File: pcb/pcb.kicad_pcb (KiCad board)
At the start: 2 copper layers, 132 x 228 mm, 54 parts, among them J1 GPS Module Breakout, J2 MicroSD Card Breakout, J3 I2C Display, J4 Exhaust Fan, U1 XIAO-ESP32-C5-DIP, U10 XIAO-ESP32-C5-DIP, U11 XIAO-ESP32-C5-DIP, U12 XIAO-ESP32-C5-DIP, U13 XIAO-ESP32-C5-DIP, U14 XIAO-ESP32-C5-DIP, U15 XIAO-ESP32-C5-DIP, U16 XIAO-ESP32-C5-DIP, U17 ESP32-S3 DevKitC-1, U18 LD1117V33, U19 SN74HC125N, U2 XIAO-ESP32-C5-DIP, U20 SN74HC138N, U21 SN74HC138N, U3 XIAO-ESP32-C5-DIP, U4 XIAO-ESP32-C5-DIP, U5 XIAO-ESP32-C5-DIP, U6 XIAO-ESP32-C5-DIP, U7 XIAO-ESP32-C5-DIP, U8 XIAO-ESP32-C5-DIP, U9 XIAO-ESP32-C5-DIP

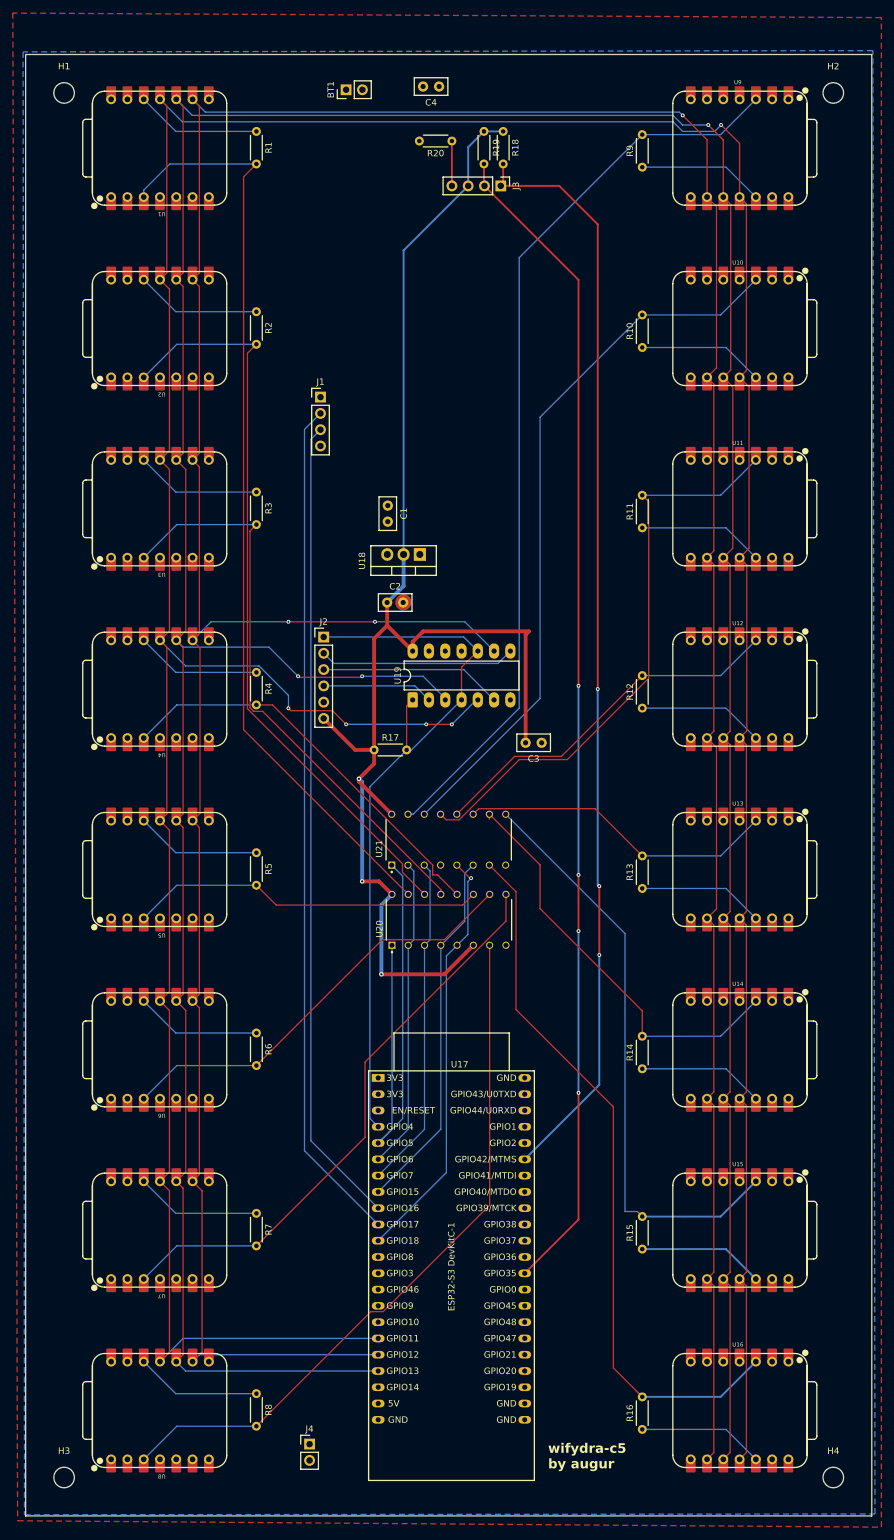
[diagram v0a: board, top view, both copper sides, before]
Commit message: Increasing ordered magic
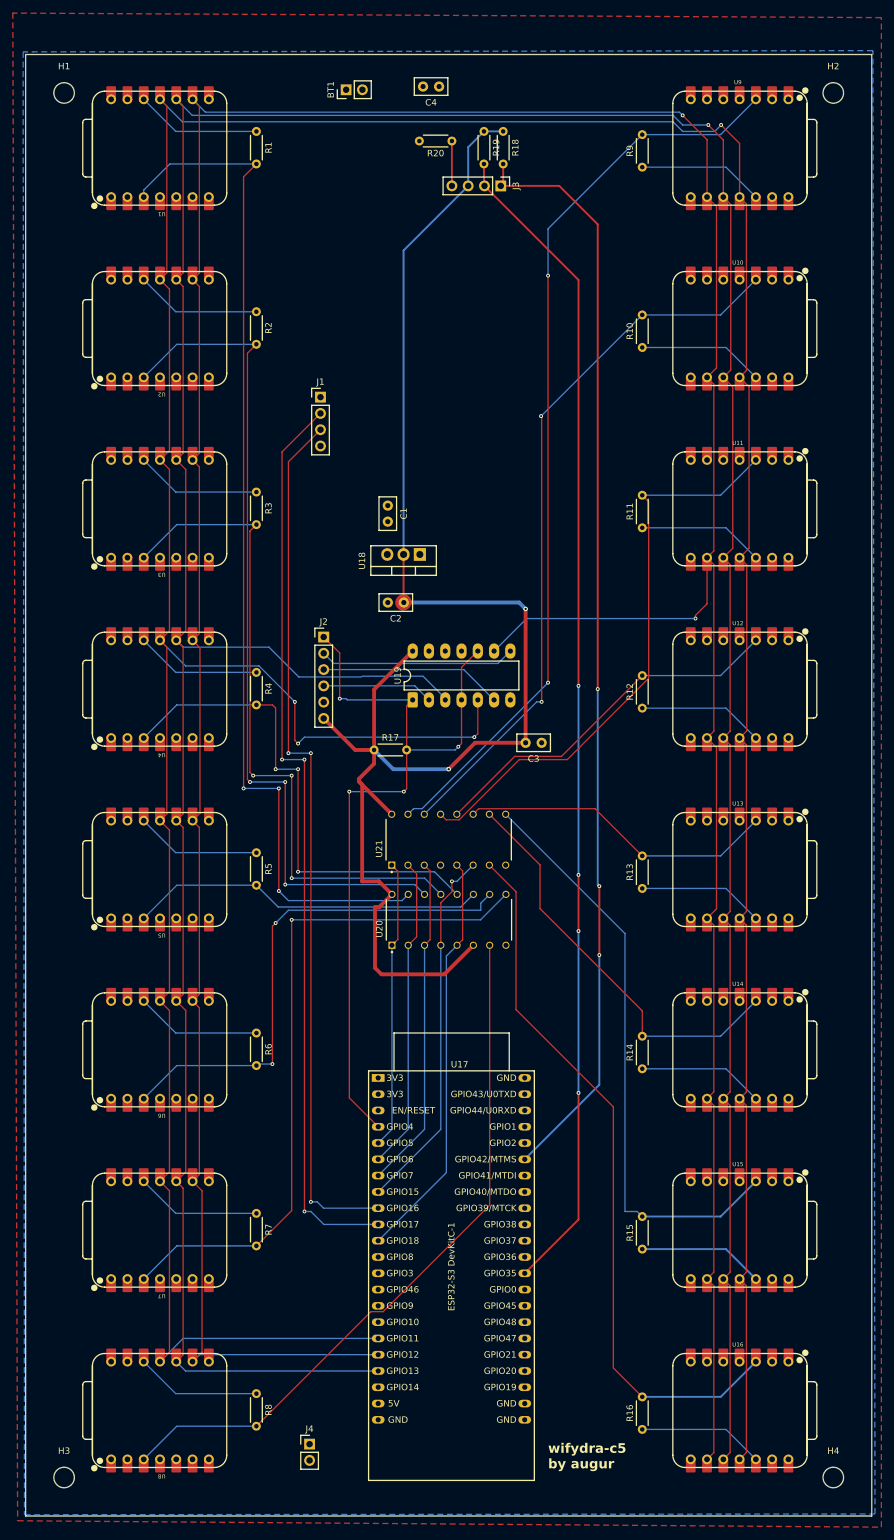
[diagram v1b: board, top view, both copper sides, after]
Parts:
- moved C2 2.60 mm to (71.0, 97.5), turned to 180 degrees
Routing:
- net /CS Addr 1: track 77.4 -> 45.0 mm
- net +3.3V: track 224.2 -> 241.6 mm, vias 3 -> 2
- net /CS 07: track 90.7 -> 107.9 mm, vias 0 -> 1
- net /CS 01: track 145.8 -> 161.3 mm, vias 0 -> 3
- net /CS 02: track 117.6 -> 132.6 mm, vias 0 -> 3
- net /CS 03: track 91.0 -> 105.8 mm, vias 0 -> 3
- net /CS 04: track 64.2 -> 78.2 mm, vias 0 -> 3
- net /CS 06: track 67.2 -> 80.4 mm, vias 0 -> 2
- net /GPS_RX: track 126.4 -> 136.9 mm, vias 0 -> 3
- net /GPS_TX: track 132.3 -> 142.8 mm, vias 0 -> 3
- net /CS 00: track 115.6 -> 124.2 mm, vias 0 -> 4
- net /MOSI: track 604.1 -> 612.2 mm, vias 5 -> 4
- net /SCK: track 578.6 -> 571.4 mm, vias 3 -> 2
- net /CS 16: track 114.2 -> 112.8 mm
- net /CS ENABLE: track 65.6 -> 64.4 mm, vias 1 -> 0
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
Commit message: Made more consistent lines
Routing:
- net /CS 14: track 64.5 -> 74.2 mm, vias 0 -> 2
- net /CS 12: track 57.9 -> 66.9 mm, vias 0 -> 1
- net /CS 15: track 92.7 -> 100.0 mm, vias 0 -> 2
- net /CS 16: track 112.8 -> 118.7 mm, vias 0 -> 2
- net /SDA: track 172.0 -> 177.5 mm, vias 3 -> 1
- net /CS 13: track 49.8 -> 54.6 mm
- net /CS 11: track 90.9 -> 95.5 mm, vias 0 -> 1
- net /SCL: vias 4 -> 0

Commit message: Attempt to center screen
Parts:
- moved R18 4.61 mm to (82.0, 25.0)
- moved R19 4.61 mm to (79.0, 25.0)
- moved R20 4.61 mm to (74.0, 26.5)
- moved J3 4.11 mm to (82.0, 33.0)
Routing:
- net +3.3V: track 241.6 -> 71.4 mm, vias 2 -> 0
- net /SCL: track 182.6 -> 193.7 mm
- net Net-(J3-Pin_4): track 7.00 -> 0.00 mm
- net /CS 09: track 141.9 -> 145.7 mm
- net /SDA: track 177.5 -> 180.7 mm

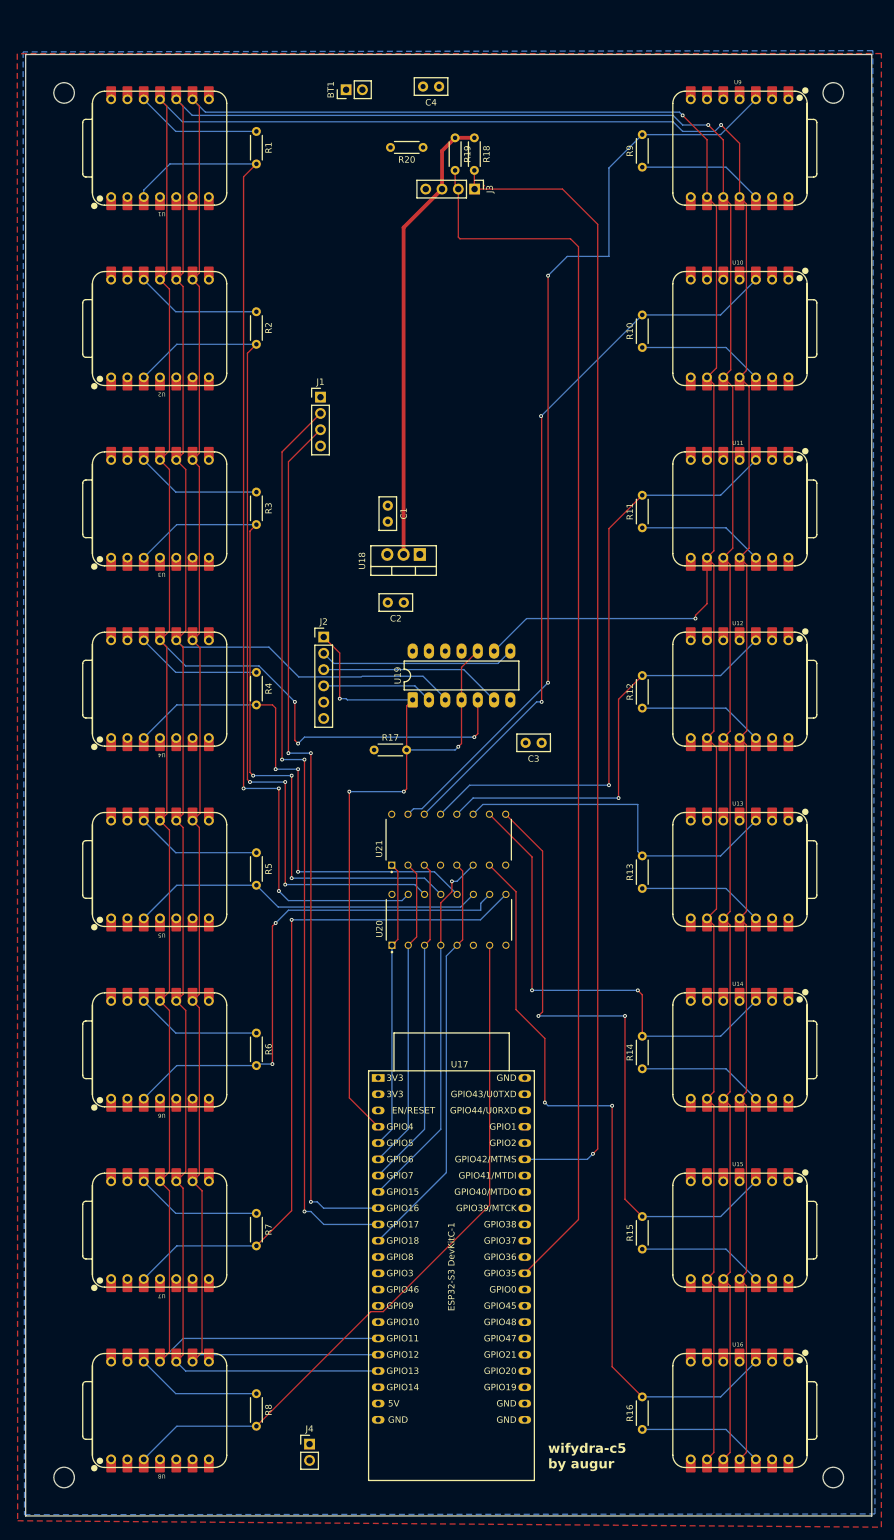
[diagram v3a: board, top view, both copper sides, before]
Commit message: Add input buttons for some future use
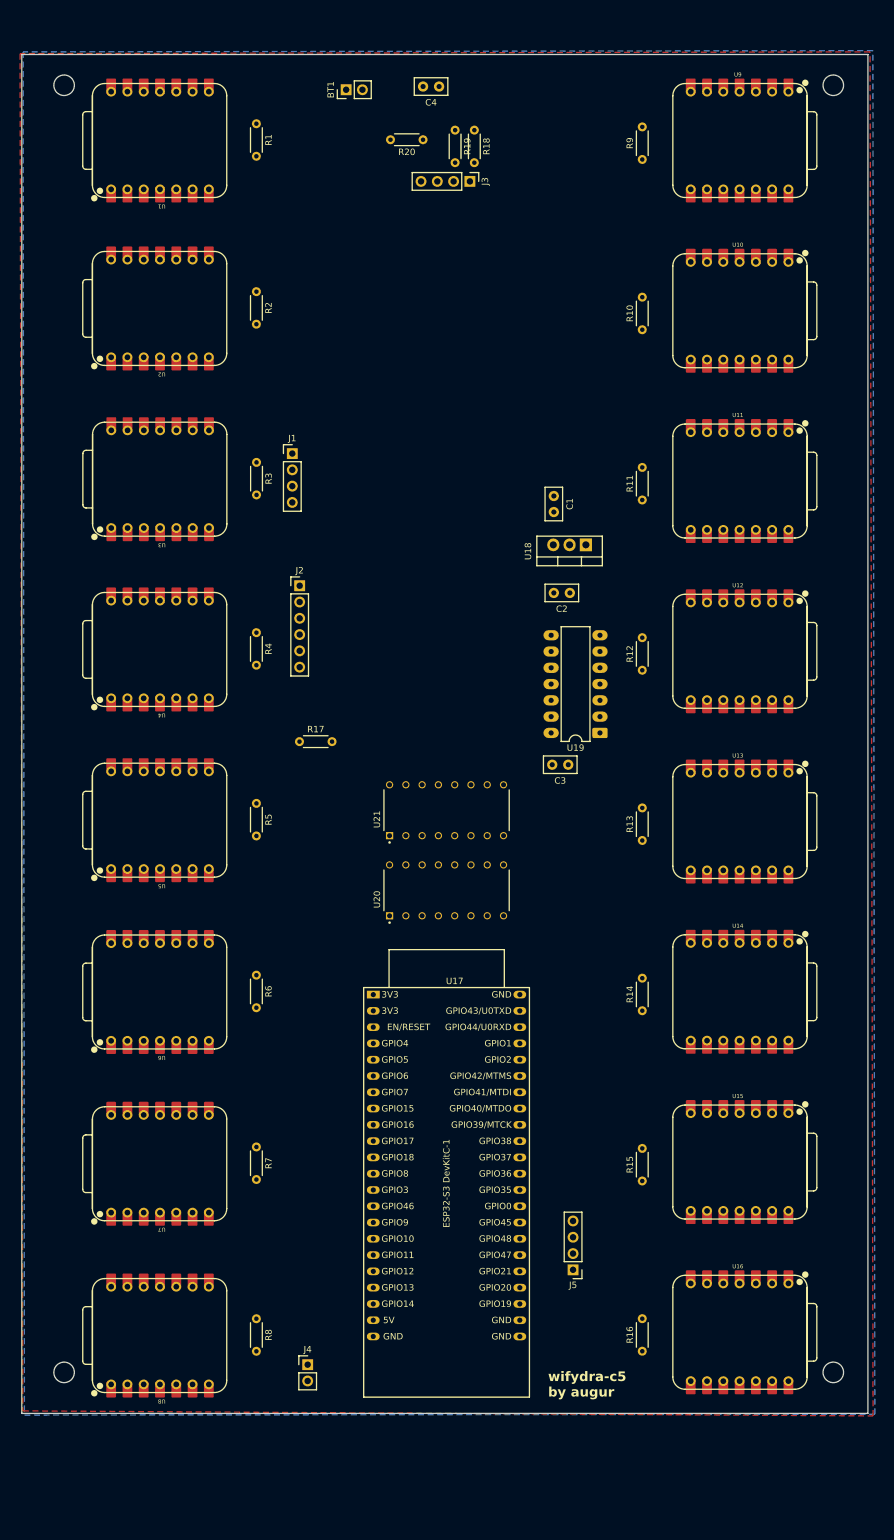
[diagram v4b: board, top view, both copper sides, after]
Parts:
- added J5: Input Buttons?, Connector_PinHeader_2.54mm:PinHeader_1x04_P2.54mm_Vertical, F.Cu at (97.4, 201.6)
- moved U19 29.7 mm to (101.6, 117.8), turned to 180 degrees
- moved C1 25.9 mm to (94.4, 80.9)
- moved C2 25.9 mm to (96.9, 96.0)
- moved U18 25.9 mm to (99.4, 88.5)
- moved H3 16.4 mm to (18.0, 217.6)
- moved H4 16.4 mm to (138.0, 217.6)
- moved U17 13.0 mm to (66.2, 158.7)
- moved J4 12.4 mm to (56.0, 216.4)
- moved R16 12.2 mm to (108.2, 214.3)
- moved U16 12.2 mm to (123.4, 211.3)
- moved R17 11.7 mm to (54.7, 119.2)
- moved R8 11.7 mm to (48.0, 209.2)
- moved U8 11.7 mm to (33.0, 211.9)
- moved R15 10.6 mm to (108.2, 187.7)
- moved U15 10.6 mm to (123.4, 184.8)
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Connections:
- U17 pad 28: unconnected-(U17-GPIO42-Pad28) -> Net-(J5-Pin_2)
- U17 pad 29: unconnected-(U17-GPIO41-Pad29) -> Net-(J5-Pin_3)
- U17 pad 30: unconnected-(U17-GPIO40-Pad30) -> Net-(J5-Pin_4)
- U17 pad 31: unconnected-(U17-GPIO39-Pad31) -> Net-(J5-Pin_5)
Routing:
- net /MOSI: track 612.2 -> 0.00 mm, vias 4 -> 0
- net /MISO: track 582.1 -> 0.00 mm, vias 1 -> 0
- net /SCK: track 571.4 -> 0.00 mm, vias 2 -> 0
- net /SCL: track 193.7 -> 0.00 mm
- net /SDA: track 180.7 -> 0.00 mm, vias 1 -> 0
- net /CS 01: track 161.3 -> 0.00 mm, vias 3 -> 0
- net /CS 09: track 145.7 -> 0.00 mm, vias 2 -> 0
- net /GPS_TX: track 142.8 -> 0.00 mm, vias 3 -> 0
- net /GPS_RX: track 136.9 -> 0.00 mm, vias 3 -> 0
- net /CS 02: track 132.6 -> 0.00 mm, vias 3 -> 0
- net /CS 00: track 124.2 -> 0.00 mm, vias 4 -> 0
- net /CS 16: track 118.7 -> 0.00 mm, vias 2 -> 0
- net /CS 10: track 112.7 -> 0.00 mm, vias 2 -> 0
- net /CS 08: track 110.9 -> 0.00 mm
- net /CS 07: track 107.9 -> 0.00 mm, vias 1 -> 0
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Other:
- board size 132 x 228 mm -> 132 x 212 mm

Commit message: First submission to pcbway!
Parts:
- moved C1 1.40 mm to (93.0, 81.0)
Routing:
- net /MOSI: track 0.00 -> 539.3 mm
- net /MISO: track 0.00 -> 529.4 mm
- net /SCK: track 0.00 -> 527.5 mm
- net +3.3V: track 0.00 -> 231.3 mm, vias 0 -> 3
- net /SCL: track 0.00 -> 174.4 mm, vias 0 -> 2
- net /SDA: track 0.00 -> 153.9 mm, vias 0 -> 2
- net /CS 09: track 0.00 -> 152.9 mm, vias 0 -> 2
- net /CS 01: track 0.00 -> 151.5 mm, vias 0 -> 2
- net /CS 00: track 0.00 -> 136.1 mm
- net /CS 02: track 0.00 -> 130.8 mm, vias 0 -> 2
- net /CS 10: track 0.00 -> 129.7 mm, vias 0 -> 1
- net /CS 16: track 0.00 -> 121.7 mm, vias 0 -> 1
- net /GPS_TX: track 0.00 -> 121.1 mm, vias 0 -> 1
- net /CS 08: track 0.00 -> 119.7 mm, vias 0 -> 1
- net /GPS_RX: track 0.00 -> 115.5 mm, vias 0 -> 1
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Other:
- board size 132 x 212 mm -> 130 x 212 mm
